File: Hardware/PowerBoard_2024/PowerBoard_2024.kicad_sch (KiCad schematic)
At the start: 218 parts, among them J1 RJ45_LED_Shielded, Q1 BSS138, Q10 BSS138, Q11 BSS138, Q12 IRF7606PBF, Q13 IRF7606PBF, Q14 SPD30P06PGBTMA1, Q15 BSS138, Q16 SPD30P06PGBTMA1, Q17 BSS138, Q18 BSS138, Q19 BSS138, Q2 IRF7606PBF, Q20 IRF7606PBF, Q21 IRF7606PBF, Q22 SPD30P06PGBTMA1, Q23 BSS138, Q24 SPD30P06PGBTMA1, Q25 BSS138, Q26 SPD30P06PGBTMA1, Q27 BSS138, Q28 SPD30P06PGBTMA1, Q29 BSS138, Q3 BSS138, Q30 SPD30P06PGBTMA1, Q4 IRF7606PBF, Q5 BSS138, Q6 SPD30P06PGBTMA1, Q7 BSS138, Q8 SPD30P06PGBTMA1, Q9 BSS138, U1 3V3, U10 ACS725xLCTR-20AB, U11 ACS725xLCTR-20AB, U12 ACS725xLCTR-20AB, U13 ACS725xLCTR-20AB, U14 ACS725xLCTR-20AB, U15 Teensy4.1_DEV-16771, U16 ACS725xLCTR-20AB, U17 ACS725xLCTR-20AB, U18 ACS725xLCTR-20AB, U19 ACS725xLCTR-20AB, U2 ACS725xLCTR-20AB, U20 PKE3316ZPI, U21 ACS725xLCTR-20AB, U22 PKE3316ZPI, U23 ACS725xLCTR-20AB, U3 ACS725xLCTR-20AB, U4 ACS725xLCTR-20AB, U5 ACS725xLCTR-20AB, U6 ACS725xLCTR-20AB, U7 ACS725xLCTR-20AB, U8 ACS725xLCTR-20AB, U9 ACS725xLCTR-20AB

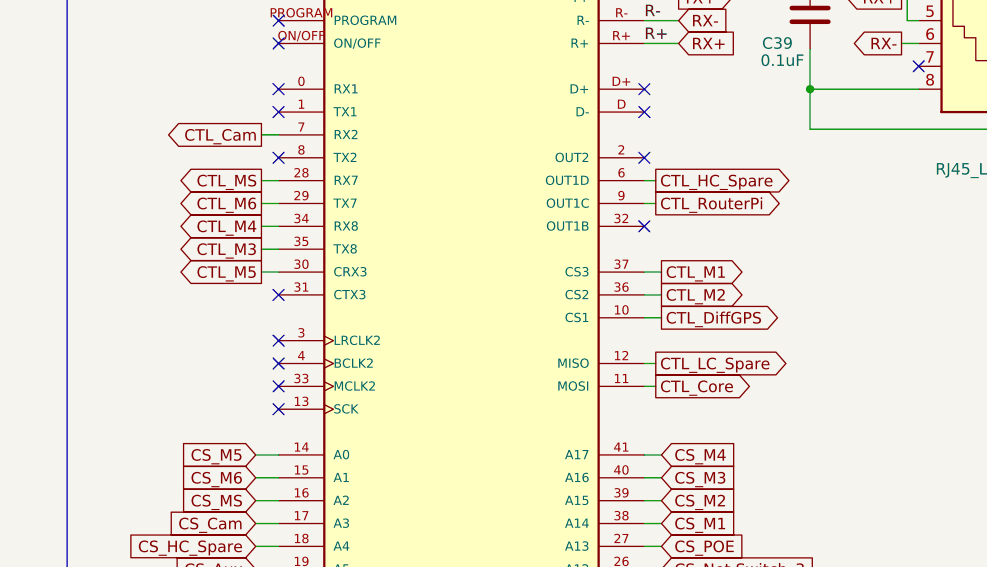
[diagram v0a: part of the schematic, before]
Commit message: Layout Changes
Changed the layout
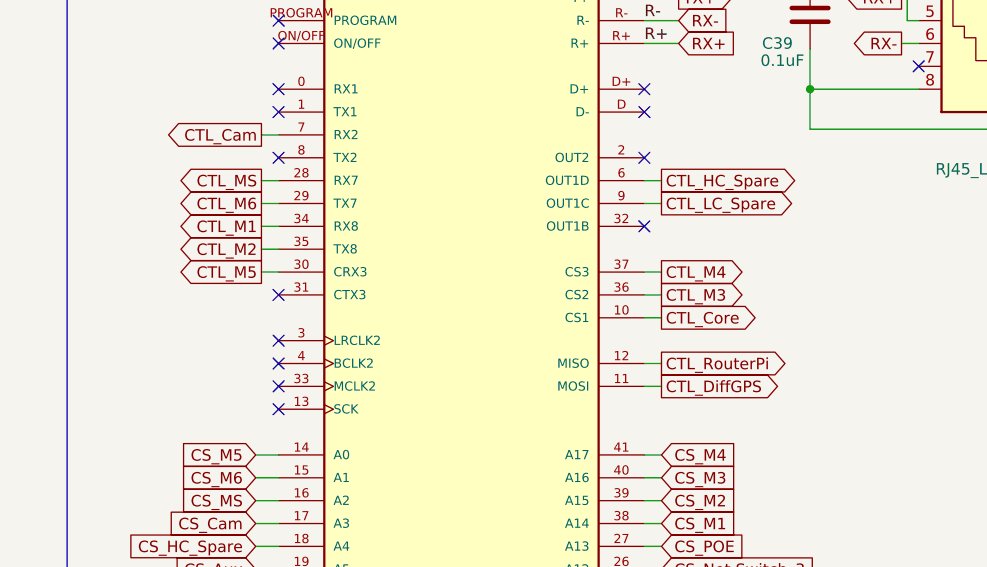
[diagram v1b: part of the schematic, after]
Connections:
- net CTL_Core: now also U15.10 (CS1); no longer U15.11 (MOSI)
- net CTL_DiffGPS: now also U15.11 (MOSI); no longer U15.10 (CS1)
- net CTL_LC_Spare: now also U15.9 (OUT1C); no longer U15.12 (MISO)
- net CTL_M1: now also U15.34 (RX8); no longer U15.37 (CS3)
- net CTL_M2: now also U15.35 (TX8); no longer U15.36 (CS2)
- net CTL_M3: now also U15.36 (CS2); no longer U15.35 (TX8)
- net CTL_M4: now also U15.37 (CS3); no longer U15.34 (RX8)
- net CTL_RouterPi: now also U15.12 (MISO); no longer U15.9 (OUT1C)
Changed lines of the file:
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@@
     (stroke (width 0) (type default))
   )
-  (wire (pts (xy 514.35 217.805) (xy 516.255 217.805))
-    (stroke (width 0) (type default))
-  )
   (wire (pts (xy 516.255 243.205) (xy 514.35 243.205))
     (stroke (width 0) (type default))
@@
     (stroke (width 0) (type default))
   )
+  (wire (pts (xy 471.805 215.265) (xy 473.71 215.265))
+    (stroke (width 0) (type default))
+  )
   (wire (pts (xy 532.765 182.245) (xy 543.56 182.245))
     (stroke (width 0) (type default))
@@
     (stroke (width 0) (type default))
   )
+  (wire (pts (xy 514.35 222.885) (xy 516.255 222.885))
+    (stroke (width 0) (type default))
+  )
   (wire (pts (xy 248.285 107.315) (xy 248.285 109.855))
     (stroke (width 0) (type default))
@@
     (stroke (width 0) (type default))
   )
-  (wire (pts (xy 471.805 215.265) (xy 473.71 215.265))
-    (stroke (width 0) (type default))
-  )
   (wire (pts (xy 526.415 121.285) (xy 537.845 121.285))
     (stroke (width 0) (type default))
@@
     (stroke (width 0) (type default))
   )
+  (wire (pts (xy 471.805 212.725) (xy 473.71 212.725))
+    (stroke (width 0) (type default))
+  )
   (wire (pts (xy 567.69 197.485) (xy 567.69 201.93))
     (stroke (width 0) (type default))
@@
     (stroke (width 0) (type default))
   )
-  (wire (pts (xy 471.805 212.725) (xy 473.71 212.725))
-    (stroke (width 0) (type default))
-  )
   (wire (pts (xy 459.105 80.645) (xy 470.535 80.645))
     (stroke (width 0) (type default))
@@
     (stroke (width 0) (type default))
   )
-  (wire (pts (xy 514.35 222.885) (xy 516.255 222.885))
-    (stroke (width 0) (type default))
-  )
   (wire (pts (xy 187.325 31.75) (xy 187.325 33.02))
     (stroke (width 0) (type default))
@@
     (stroke (width 0) (type default))
   )
-  (wire (pts (xy 515.62 227.965) (xy 514.35 227.965))
+  (wire (pts (xy 441.96 43.815) (xy 446.405 43.815))
     (stroke (width 0) (type default))
   )
-  (wire (pts (xy 441.96 43.815) (xy 446.405 43.815))
+  (wire (pts (xy 514.35 230.505) (xy 516.255 230.505))
     (stroke (width 0) (type default))
   )
@@
     (stroke (width 0) (type default))
   )
+  (wire (pts (xy 514.35 210.185) (xy 516.255 210.185))
+    (stroke (width 0) (type default))
+  )
   (wire (pts (xy 307.975 44.45) (xy 312.42 44.45))
     (stroke (width 0) (type default))
@@
     (stroke (width 0) (type default))
   )
-  (wire (pts (xy 514.35 230.505) (xy 515.62 230.505))
-    (stroke (width 0) (type default))
-  )
   (wire (pts (xy 307.975 55.245) (xy 307.975 56.515))
     (stroke (width 0) (type default))
@@
     (stroke (width 0) (type default))
   )
+  (wire (pts (xy 514.35 220.345) (xy 516.255 220.345))
+    (stroke (width 0) (type default))
+  )
   (wire (pts (xy 128.27 31.75) (xy 128.27 34.29))
     (stroke (width 0) (type default))
@@
     (stroke (width 0) (type default))
   )
-  (wire (pts (xy 514.35 207.645) (xy 515.62 207.645))
+  (wire (pts (xy 514.35 207.645) (xy 516.255 207.645))
     (stroke (width 0) (type default))
   )
@@
     (stroke (width 0) (type default))
   )
+  (wire (pts (xy 514.35 217.805) (xy 516.255 217.805))
+    (stroke (width 0) (type default))
+  )
   (wire (pts (xy 470.535 97.79) (xy 474.98 97.79))
     (stroke (width 0) (type default))
@@
     (stroke (width 0) (type default))
   )
-  (wire (pts (xy 514.35 220.345) (xy 516.255 220.345))
-    (stroke (width 0) (type default))
-  )
   (wire (pts (xy 296.545 37.465) (xy 296.545 38.735))
     (stroke (width 0) (type default))
@@
     (stroke (width 0) (type default))
   )
-  (wire (pts (xy 514.35 210.185) (xy 515.62 210.185))
-    (stroke (width 0) (type default))
-  )
   (wire (pts (xy 398.145 188.595) (xy 398.145 189.865))
     (stroke (width 0) (type default))
@@
     (stroke (width 0) (type default))
   )
+  (wire (pts (xy 514.35 227.965) (xy 516.255 227.965))
+    (stroke (width 0) (type default))
+  )
   (wire (pts (xy 117.475 317.5) (xy 117.475 316.23))
     (stroke (width 0) (type default))
@@
     )
   )
-  (global_label "CTL_M1" (shape output) (at 516.255 217.805 0) (fields_autoplaced)
-    (effects (font (size 1.27 1.27)) (justify left))
-    (property "Intersheetrefs" "${INTERSHEET_REFS}" (at 526.1344 217.805 0)
-      (effects (font (size 1.27 1.27)) (justify left) hide)
+  (global_label "CTL_M1" (shape output) (at 471.805 212.725 180) (fields_autoplaced)
+    (effects (font (size 1.27 1.27)) (justify right))
+    (property "Intersheetrefs" "${INTERSHEET_REFS}" (at 461.9256 212.725 0)
+      (effects (font (size 1.27 1.27)) (justify right) hide)
     )
   )
@@
     )
   )
-  (global_label "CTL_LC_Spare" (shape output) (at 515.62 227.965 0) (fields_autoplaced)
+  (global_label "CTL_LC_Spare" (shape output) (at 516.255 210.185 0) (fields_autoplaced)
     (effects (font (size 1.27 1.27)) (justify left))
-    (property "Intersheetrefs" "${INTERSHEET_REFS}" (at 530.9145 228.0444 0)
+    (property "Intersheetrefs" "${INTERSHEET_REFS}" (at 531.5495 210.2644 0)
       (effects (font (size 1.27 1.27)) (justify left) hide)
     )
@@
     )
   )
-  (global_label "CTL_M3" (shape output) (at 471.805 215.265 180) (fields_autoplaced)
-    (effects (font (size 1.27 1.27)) (justify right))
-    (property "Intersheetrefs" "${INTERSHEET_REFS}" (at 461.9256 215.265 0)
-      (effects (font (size 1.27 1.27)) (justify right) hide)
+  (global_label "CTL_M3" (shape output) (at 516.255 220.345 0) (fields_autoplaced)
+    (effects (font (size 1.27 1.27)) (justify left))
+    (property "Intersheetrefs" "${INTERSHEET_REFS}" (at 526.1344 220.345 0)
+      (effects (font (size 1.27 1.27)) (justify left) hide)
     )
   )
@@
     )
   )
-  (global_label "CTL_M4" (shape output) (at 471.805 212.725 180) (fields_autoplaced)
-    (effects (font (size 1.27 1.27)) (justify right))
-    (property "Intersheetrefs" "${INTERSHEET_REFS}" (at 461.9256 212.725 0)
-      (effects (font (size 1.27 1.27)) (justify right) hide)
+  (global_label "CTL_M4" (shape output) (at 516.255 217.805 0) (fields_autoplaced)
+    (effects (font (size 1.27 1.27)) (justify left))
+    (property "Intersheetrefs" "${INTERSHEET_REFS}" (at 526.1344 217.805 0)
+      (effects (font (size 1.27 1.27)) (justify left) hide)
     )
   )
@@
     )
   )
-  (global_label "CTL_Core" (shape output) (at 515.62 230.505 0) (fields_autoplaced)
+  (global_label "CTL_Core" (shape output) (at 516.255 222.885 0) (fields_autoplaced)
     (effects (font (size 1.27 1.27)) (justify left))
-    (property "Intersheetrefs" "${INTERSHEET_REFS}" (at 527.1323 230.505 0)
+    (property "Intersheetrefs" "${INTERSHEET_REFS}" (at 527.7673 222.885 0)
       (effects (font (size 1.27 1.27)) (justify left) hide)
     )
@@
     )
   )
-  (global_label "CTL_RouterPi" (shape output) (at 515.62 210.185 0) (fields_autoplaced)
+  (global_label "CTL_RouterPi" (shape output) (at 516.255 227.965 0) (fields_autoplaced)
     (effects (font (size 1.27 1.27)) (justify left))
-    (property "Intersheetrefs" "${INTERSHEET_REFS}" (at 530.8818 210.185 0)
+    (property "Intersheetrefs" "${INTERSHEET_REFS}" (at 531.5168 227.965 0)
       (effects (font (size 1.27 1.27)) (justify left) hide)
     )
@@
     )
   )
-  (global_label "CTL_HC_Spare" (shape output) (at 515.62 207.645 0) (fields_autoplaced)
+  (global_label "CTL_HC_Spare" (shape output) (at 516.255 207.645 0) (fields_autoplaced)
     (effects (font (size 1.27 1.27)) (justify left))
-    (property "Intersheetrefs" "${INTERSHEET_REFS}" (at 531.7889 207.645 0)
+    (property "Intersheetrefs" "${INTERSHEET_REFS}" (at 532.4239 207.645 0)
       (effects (font (size 1.27 1.27)) (justify left) hide)
     )
@@
     )
   )
-  (global_label "CTL_M2" (shape output) (at 516.255 220.345 0) (fields_autoplaced)
-    (effects (font (size 1.27 1.27)) (justify left))
-    (property "Intersheetrefs" "${INTERSHEET_REFS}" (at 526.1344 220.345 0)
-      (effects (font (size 1.27 1.27)) (justify left) hide)
+  (global_label "CTL_M2" (shape output) (at 471.805 215.265 180) (fields_autoplaced)
+    (effects (font (size 1.27 1.27)) (justify right))
+    (property "Intersheetrefs" "${INTERSHEET_REFS}" (at 461.9256 215.265 0)
+      (effects (font (size 1.27 1.27)) (justify right) hide)
     )
   )
@@
     )
   )
-  (global_label "CTL_DiffGPS" (shape output) (at 516.255 222.885 0) (fields_autoplaced)
+  (global_label "CTL_DiffGPS" (shape output) (at 516.255 230.505 0) (fields_autoplaced)
     (effects (font (size 1.27 1.27)) (justify left))
-    (property "Intersheetrefs" "${INTERSHEET_REFS}" (at 530.5492 222.885 0)
+    (property "Intersheetrefs" "${INTERSHEET_REFS}" (at 530.5492 230.505 0)
       (effects (font (size 1.27 1.27)) (justify left) hide)
     )

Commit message: Layout Review Ready
Made the traces pretty
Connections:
- net CS_Core: now also U15.22 (A8); no longer U15.21 (A7)
- net CS_DiffGPS: now also U15.21 (A7); no longer U15.22 (A8)
- net CS_LC_Spare: now also U15.23 (A9); no longer U15.20 (A6)
- net CS_RouterPi: now also U15.20 (A6); no longer U15.23 (A9)
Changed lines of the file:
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@@
     (stroke (width 0) (type default))
   )
+  (wire (pts (xy 471.17 255.905) (xy 473.71 255.905))
+    (stroke (width 0) (type default))
+  )
   (wire (pts (xy 403.225 117.475) (xy 403.225 121.285))
     (stroke (width 0) (type default))
@@
     (stroke (width 0) (type default))
   )
+  (wire (pts (xy 514.35 258.445) (xy 516.255 258.445))
+    (stroke (width 0) (type default))
+  )
   (wire (pts (xy 562.61 111.125) (xy 562.61 105.41))
     (stroke (width 0) (type default))
@@
     (stroke (width 0) (type default))
   )
-  (wire (pts (xy 471.17 255.905) (xy 473.71 255.905))
-    (stroke (width 0) (type default))
-  )
   (wire (pts (xy 375.285 64.135) (xy 375.285 67.945))
     (stroke (width 0) (type default))
@@
     (stroke (width 0) (type default))
   )
+  (wire (pts (xy 471.17 253.365) (xy 473.71 253.365))
+    (stroke (width 0) (type default))
+  )
   (wire (pts (xy 322.58 36.195) (xy 322.58 34.29))
     (stroke (width 0) (type default))
@@
     (stroke (width 0) (type default))
   )
-  (wire (pts (xy 471.17 253.365) (xy 473.71 253.365))
-    (stroke (width 0) (type default))
-  )
   (wire (pts (xy 202.565 39.37) (xy 210.82 39.37))
     (stroke (width 0) (type default))
@@
     (stroke (width 0) (type default))
   )
-  (wire (pts (xy 514.35 258.445) (xy 516.255 258.445))
-    (stroke (width 0) (type default))
-  )
   (wire (pts (xy 361.315 118.745) (xy 361.315 121.285))
     (stroke (width 0) (type default))
@@
     (stroke (width 0) (type default))
   )
-  (wire (pts (xy 471.17 258.445) (xy 473.71 258.445))
-    (stroke (width 0) (type default))
-  )
   (wire (pts (xy 389.89 67.945) (xy 400.05 67.945))
     (stroke (width 0) (type default))
@@
     (stroke (width 0) (type default))
   )
+  (wire (pts (xy 471.17 258.445) (xy 473.71 258.445))
+    (stroke (width 0) (type default))
+  )
   (wire (pts (xy 154.305 187.325) (xy 154.305 189.865))
     (stroke (width 0) (type default))
@@
     )
   )
-  (global_label "CS_Core" (shape input) (at 471.17 255.905 180) (fields_autoplaced)
+  (global_label "CS_Core" (shape input) (at 471.17 258.445 180) (fields_autoplaced)
     (effects (font (size 1.27 1.27)) (justify right))
-    (property "Intersheetrefs" "${INTERSHEET_REFS}" (at 460.4439 255.905 0)
+    (property "Intersheetrefs" "${INTERSHEET_REFS}" (at 460.4439 258.445 0)
       (effects (font (size 1.27 1.27)) (justify right) hide)
     )
@@
     )
   )
-  (global_label "CS_RouterPi" (shape input) (at 516.255 258.445 0) (fields_autoplaced)
-    (effects (font (size 1.27 1.27)) (justify left))
-    (property "Intersheetrefs" "${INTERSHEET_REFS}" (at 530.7306 258.445 0)
-      (effects (font (size 1.27 1.27)) (justify left) hide)
+  (global_label "CS_RouterPi" (shape input) (at 471.17 253.365 180) (fields_autoplaced)
+    (effects (font (size 1.27 1.27)) (justify right))
+    (property "Intersheetrefs" "${INTERSHEET_REFS}" (at 456.6944 253.365 0)
+      (effects (font (size 1.27 1.27)) (justify right) hide)
     )
   )
@@
     )
   )
-  (global_label "CS_DiffGPS" (shape input) (at 471.17 258.445 180) (fields_autoplaced)
+  (global_label "CS_DiffGPS" (shape input) (at 471.17 255.905 180) (fields_autoplaced)
     (effects (font (size 1.27 1.27)) (justify right))
-    (property "Intersheetrefs" "${INTERSHEET_REFS}" (at 457.662 258.445 0)
+    (property "Intersheetrefs" "${INTERSHEET_REFS}" (at 457.662 255.905 0)
       (effects (font (size 1.27 1.27)) (justify right) hide)
     )
@@
     )
   )
-  (global_label "CS_LC_Spare" (shape input) (at 471.17 253.365 180) (fields_autoplaced)
-    (effects (font (size 1.27 1.27)) (justify right))
-    (property "Intersheetrefs" "${INTERSHEET_REFS}" (at 456.0897 253.365 0)
-      (effects (font (size 1.27 1.27)) (justify right) hide)
+  (global_label "CS_LC_Spare" (shape input) (at 516.255 258.445 0) (fields_autoplaced)
+    (effects (font (size 1.27 1.27)) (justify left))
+    (property "Intersheetrefs" "${INTERSHEET_REFS}" (at 531.3353 258.445 0)
+      (effects (font (size 1.27 1.27)) (justify left) hide)
     )
   )

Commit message: Fixed planes
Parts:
- U10, U11, U18, U19, U2, U3, U6, U7: footprint Package_SO:SOIC-8_3.9x4.9mm_P1.27mm -> Package_SO:SOP-8_3.9x4.9mm_P1.27mm
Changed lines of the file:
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@@
       (effects (font (size 1.27 1.27)) (justify left))
     )
-    (property "Footprint" "Package_SO:SOIC-8_3.9x4.9mm_P1.27mm" (at 252.73 198.12 0)
+    (property "Footprint" "Package_SO:SOP-8_3.9x4.9mm_P1.27mm" (at 252.73 198.12 0)
       (effects (font (size 1.27 1.27) italic) (justify left) hide)
     )
@@
       (effects (font (size 1.27 1.27)) (justify left))
     )
-    (property "Footprint" "Package_SO:SOIC-8_3.9x4.9mm_P1.27mm" (at 347.345 203.2 0)
+    (property "Footprint" "Package_SO:SOP-8_3.9x4.9mm_P1.27mm" (at 347.345 203.2 0)
       (effects (font (size 1.27 1.27) italic) (justify left) hide)
     )
@@
       (effects (font (size 1.27 1.27)) (justify left))
     )
-    (property "Footprint" "Package_SO:SOIC-8_3.9x4.9mm_P1.27mm" (at 415.925 202.565 0)
+    (property "Footprint" "Package_SO:SOP-8_3.9x4.9mm_P1.27mm" (at 415.925 202.565 0)
       (effects (font (size 1.27 1.27) italic) (justify left) hide)
     )
@@
       (effects (font (size 1.27 1.27)) (justify left))
     )
-    (property "Footprint" "Package_SO:SOIC-8_3.9x4.9mm_P1.27mm" (at 217.17 250.825 0)
+    (property "Footprint" "Package_SO:SOP-8_3.9x4.9mm_P1.27mm" (at 217.17 250.825 0)
       (effects (font (size 1.27 1.27) italic) (justify left) hide)
     )
@@
       (effects (font (size 1.27 1.27)) (justify left))
     )
-    (property "Footprint" "Package_SO:SOIC-8_3.9x4.9mm_P1.27mm" (at 415.925 254 0)
+    (property "Footprint" "Package_SO:SOP-8_3.9x4.9mm_P1.27mm" (at 415.925 254 0)
       (effects (font (size 1.27 1.27) italic) (justify left) hide)
     )
@@
       (effects (font (size 1.27 1.27)) (justify left))
     )
-    (property "Footprint" "Package_SO:SOIC-8_3.9x4.9mm_P1.27mm" (at 348.615 254 0)
+    (property "Footprint" "Package_SO:SOP-8_3.9x4.9mm_P1.27mm" (at 348.615 254 0)
       (effects (font (size 1.27 1.27) italic) (justify left) hide)
     )
@@
       (effects (font (size 1.27 1.27)) (justify left))
     )
-    (property "Footprint" "Package_SO:SOIC-8_3.9x4.9mm_P1.27mm" (at 171.45 250.825 0)
+    (property "Footprint" "Package_SO:SOP-8_3.9x4.9mm_P1.27mm" (at 171.45 250.825 0)
       (effects (font (size 1.27 1.27) italic) (justify left) hide)
     )
@@
       (effects (font (size 1.27 1.27)) (justify left))
     )
-    (property "Footprint" "Package_SO:SOIC-8_3.9x4.9mm_P1.27mm" (at 182.88 197.485 0)
+    (property "Footprint" "Package_SO:SOP-8_3.9x4.9mm_P1.27mm" (at 182.88 197.485 0)
       (effects (font (size 1.27 1.27) italic) (justify left) hide)
     )

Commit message: I changed the C6 to 1206 from 0603
cap rated 35v, sees PV = needed to change cap = must alter footprint
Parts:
- C6: footprint Capacitor_SMD:C_0603_1608Metric_Pad1.08x0.95mm_HandSolder -> Capacitor_SMD:C_1206_3216Metric_Pad1.33x1.80mm_HandSolder
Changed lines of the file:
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@@
       (effects (font (size 1.27 1.27)) (justify left))
     )
-    (property "Footprint" "Capacitor_SMD:C_0603_1608Metric_Pad1.08x0.95mm_HandSolder" (at 42.545 81.915 0)
+    (property "Footprint" "Capacitor_SMD:C_1206_3216Metric_Pad1.33x1.80mm_HandSolder" (at 42.545 81.915 0)
       (effects (font (size 1.27 1.27)) hide)
     )
